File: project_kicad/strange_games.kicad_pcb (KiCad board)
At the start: 2 copper layers, 166 x 166 mm, 210 parts, among them J1 Display, M1 Motor_DC, Q1 Si2302A, Q3 Si2302A, Q4 Q_Photo, SW1 SW_Push, SW10 SW_Push, SW11 SW_Push, SW2 SW_Push, SW3 SW_Push, SW4 SW_Push, SW5 SW_Push, SW6 SW_Push, SW7 SW_Push, SW8 SW_Push, SW9 SW_Push, U1 charge controller, U2 boost converter, U3 LDL1117S33R, U4 ESP32-DEVKIT-V1, U5 TMP112xxDRL, U6 vibrating_sensor, U7 LSM6DS3, U8 MQ-135 gas sensor

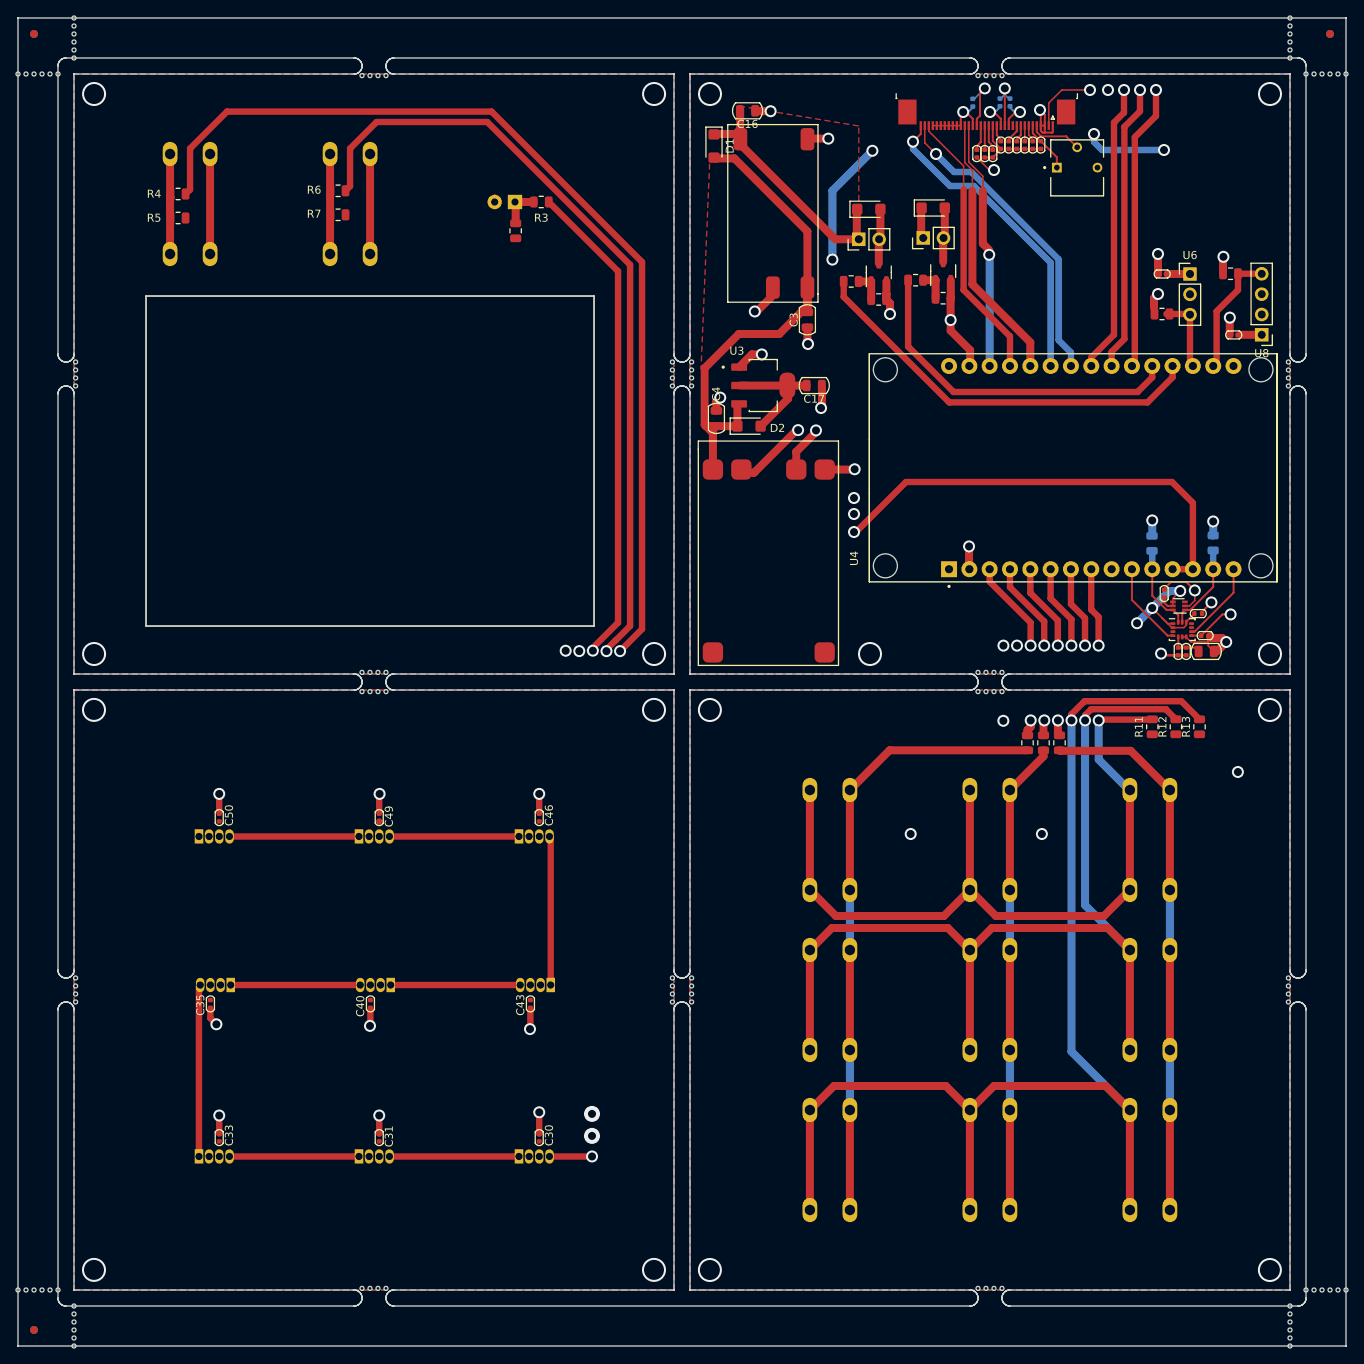
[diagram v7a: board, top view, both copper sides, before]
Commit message: bugfix
In the last version we lost netlist - it was improved
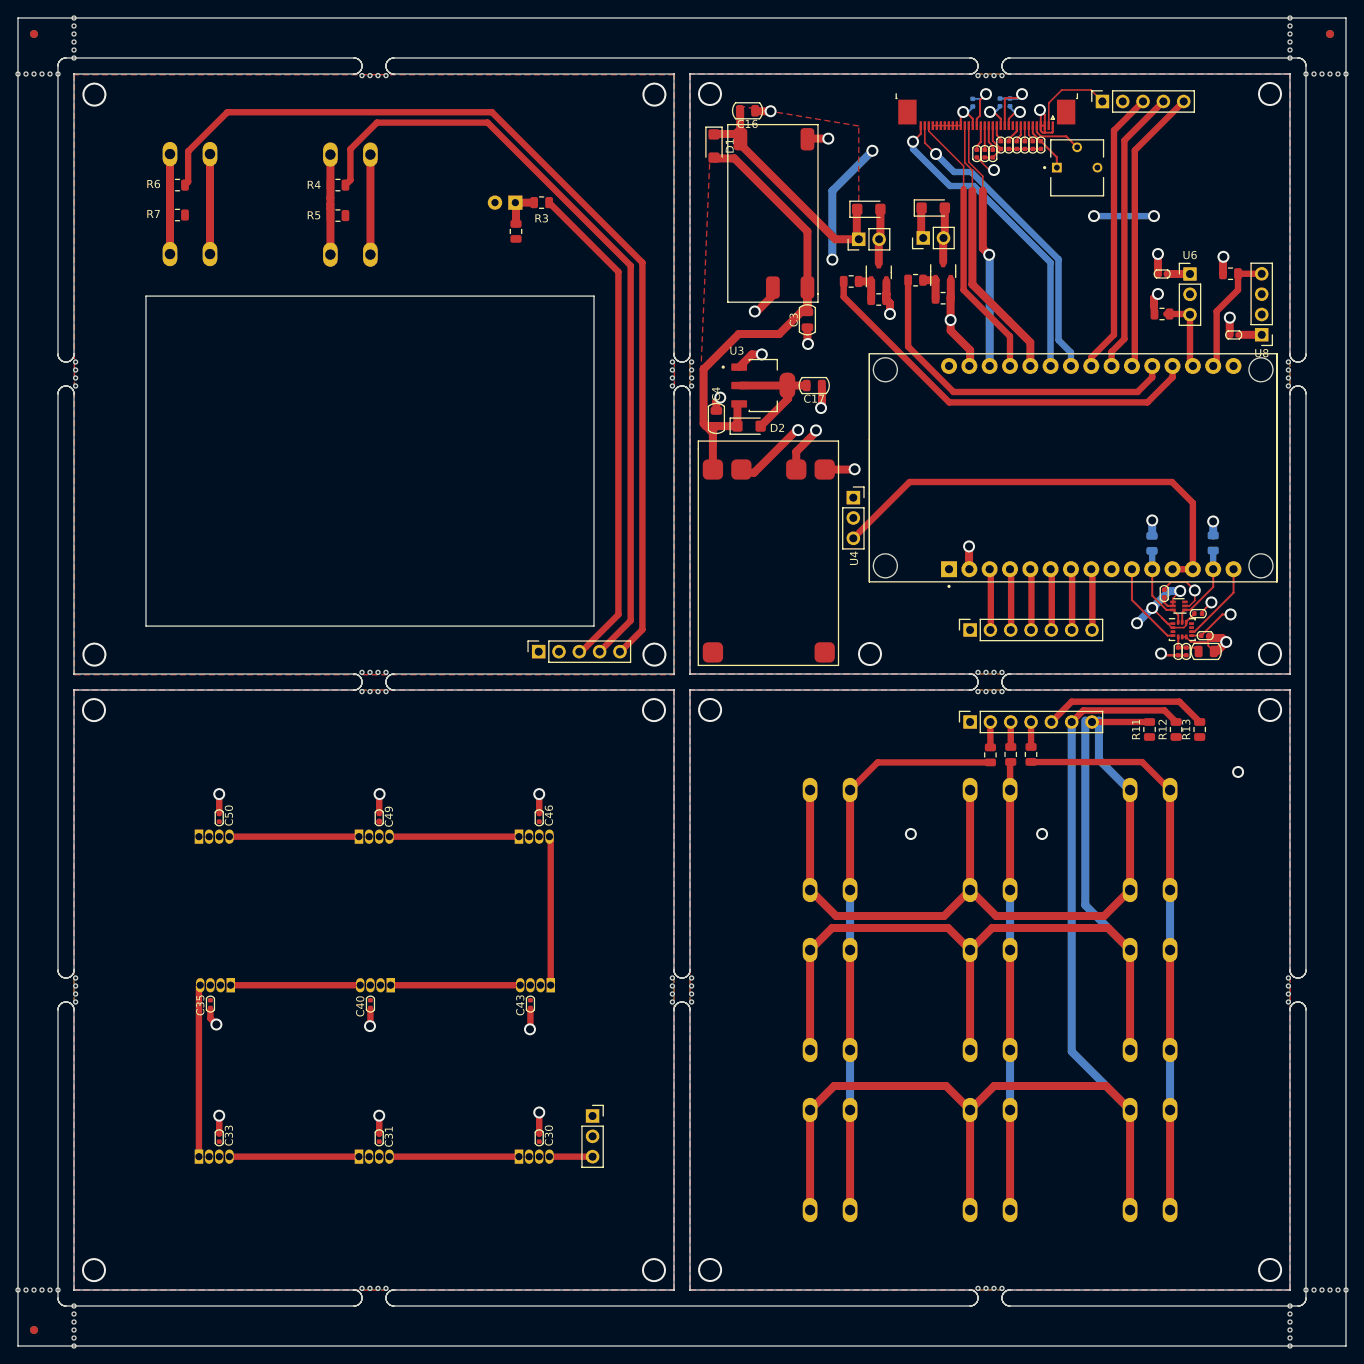
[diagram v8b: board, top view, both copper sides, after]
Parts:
- added REF**: PinSocket_1x07_P2.54mm_Vertical, Connector_PinSocket_2.54mm:PinSocket_1x07_P2.54mm_Vertical, F.Cu at (163.0, 96.5)
- added REF**: PinSocket_1x07_P2.54mm_Vertical, Connector_PinSocket_2.54mm:PinSocket_1x07_P2.54mm_Vertical, F.Cu at (163.0, 108.0)
- added REF**: PinSocket_1x05_P2.54mm_Vertical, Connector_PinSocket_2.54mm:PinSocket_1x05_P2.54mm_Vertical, F.Cu at (109.1, 99.2)
- added REF**: PinSocket_1x03_P2.54mm_Vertical, Connector_PinSocket_2.54mm:PinSocket_1x03_P2.54mm_Vertical, F.Cu at (148.4, 80.0)
- added REF**: PinSocket_1x03_P2.54mm_Vertical, Connector_PinSocket_2.54mm:PinSocket_1x03_P2.54mm_Vertical, F.Cu at (115.8, 157.3)
- added REF**: PinSocket_1x05_P2.54mm_Vertical, Connector_PinSocket_2.54mm:PinSocket_1x05_P2.54mm_Vertical, F.Cu at (179.6, 30.4)
- moved R6 20.1 mm to (63.9, 40.9)
- moved R7 20.1 mm to (63.9, 44.6)
- moved SW1 20.0 mm to (83.1, 37.1)
- moved R4 20.0 mm to (84.0, 40.9)
- moved SW2 20.0 mm to (63.0, 37.0)
- moved R5 20.0 mm to (84.0, 44.7)
- moved R8 4.88 mm to (165.6, 112.1)
- moved R9 4.35 mm to (168.1, 112.1)
- moved R10 3.84 mm to (170.6, 112.1)
- moved R11 0.48 mm to (185.4, 108.9)
- moved R13 0.34 mm to (191.7, 108.9)
- moved R12 0.34 mm to (188.8, 108.9)
- moved R20 0.09 mm to (106.3, 46.7)
- moved R3 0.09 mm to (109.5, 43.1)
- moved Q4 0.09 mm to (106.2, 43.1)
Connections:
- C30 pad 1: (no net) -> GND
- C30 pad 2: (no net) -> +3V3
- C31 pad 1: (no net) -> +3V3
- C31 pad 2: (no net) -> GND
- C33 pad 1: (no net) -> GND
- C33 pad 2: (no net) -> +3V3
- C35 pad 1: (no net) -> +3V3
- C35 pad 2: (no net) -> GND
- C40 pad 1: (no net) -> GND
- C40 pad 2: (no net) -> +3V3
- C43 pad 1: (no net) -> +3V3
- C43 pad 2: (no net) -> GND
- C46 pad 1: (no net) -> GND
- C46 pad 2: (no net) -> +3V3
- C49 pad 1: (no net) -> +3V3
- C49 pad 2: (no net) -> GND
- C50 pad 1: (no net) -> GND
- C50 pad 2: (no net) -> +3V3
- D10 pad 1: (no net) -> Net-(D10-DO)
- D10 pad 2: (no net) -> GND
- D10 pad 3: (no net) -> +3V3
- D10 pad 4: (no net) -> Net-(D10-DI)
- D11 pad 1: (no net) -> Net-(D11-DO)
- D11 pad 2: (no net) -> GND
- D11 pad 3: (no net) -> +3V3
- D11 pad 4: (no net) -> Net-(D10-DO)
- D12 pad 1: (no net) -> Net-(D12-DO)
- D12 pad 2: (no net) -> GND
- D12 pad 3: (no net) -> +3V3
- D12 pad 4: (no net) -> Net-(D11-DO)
- D13 pad 1: (no net) -> unconnected-(D13-DO-Pad1)
- D13 pad 2: (no net) -> GND
- D13 pad 3: (no net) -> +3V3
- D13 pad 4: (no net) -> Net-(D12-DO)
- D5 pad 1: (no net) -> Net-(D5-DO)
- D5 pad 2: (no net) -> GND
- D5 pad 3: (no net) -> +3V3
- D5 pad 4: (no net) -> Luminodiodes
- D6 pad 1: (no net) -> Net-(D6-DO)
- D6 pad 2: (no net) -> GND
- D6 pad 3: (no net) -> +3V3
- D6 pad 4: (no net) -> Net-(D5-DO)
- D7 pad 1: (no net) -> Net-(D7-DO)
- D7 pad 2: (no net) -> GND
- D7 pad 3: (no net) -> +3V3
- D7 pad 4: (no net) -> Net-(D6-DO)
- D8 pad 1: (no net) -> Net-(D8-DO)
- D8 pad 2: (no net) -> GND
- D8 pad 3: (no net) -> +3V3
- D8 pad 4: (no net) -> Net-(D7-DO)
- D9 pad 1: (no net) -> Net-(D10-DI)
- D9 pad 2: (no net) -> GND
- D9 pad 3: (no net) -> +3V3
- D9 pad 4: (no net) -> Net-(D8-DO)
- Q4 pad 1: (no net) -> Net-(Q4-C)
- Q4 pad 2: (no net) -> GND
- R10 pad 1: (no net) -> Net-(R10-Pad1)
- R10 pad 2: (no net) -> BOut3
- R11 pad 1: (no net) -> GND
- R11 pad 2: (no net) -> Bin1
- R12 pad 1: (no net) -> GND
- R12 pad 2: (no net) -> Bin2
- R13 pad 1: (no net) -> GND
- R13 pad 2: (no net) -> Bin3
- R20 pad 1: (no net) -> Net-(Q4-C)
- R20 pad 2: (no net) -> +3V3
- R3 pad 1: (no net) -> Net-(Q4-C)
- R3 pad 2: (no net) -> PhotoSensor
- R4 pad 1: (no net) -> Net-(R4-Pad1)
- R4 pad 2: (no net) -> B1
- R5 pad 1: (no net) -> Net-(R4-Pad1)
- R5 pad 2: (no net) -> +3V3
- R6 pad 1: (no net) -> Net-(R6-Pad1)
- R6 pad 2: (no net) -> B2
- R7 pad 1: (no net) -> Net-(R6-Pad1)
- R7 pad 2: (no net) -> +3V3
- R8 pad 1: (no net) -> Net-(R8-Pad1)
- R8 pad 2: (no net) -> BOut1
- R9 pad 1: (no net) -> Net-(R9-Pad1)
- R9 pad 2: (no net) -> BOut2
- SW1 pad 1: (no net) -> Net-(R4-Pad1)
- SW1 pad 2: (no net) -> GND
- SW10 pad 1: (no net) -> Bin3
- SW10 pad 2: (no net) -> Net-(R9-Pad1)
- SW11 pad 1: (no net) -> Bin3
- SW11 pad 2: (no net) -> Net-(R10-Pad1)
- SW2 pad 1: (no net) -> Net-(R6-Pad1)
- SW2 pad 2: (no net) -> GND
- SW3 pad 1: (no net) -> Bin1
- SW3 pad 2: (no net) -> Net-(R8-Pad1)
- SW4 pad 1: (no net) -> Bin1
- SW4 pad 2: (no net) -> Net-(R9-Pad1)
- SW5 pad 1: (no net) -> Bin1
- SW5 pad 2: (no net) -> Net-(R10-Pad1)
- SW6 pad 1: (no net) -> Bin2
- SW6 pad 2: (no net) -> Net-(R8-Pad1)
- SW7 pad 1: (no net) -> Bin2
- SW7 pad 2: (no net) -> Net-(R9-Pad1)
- SW8 pad 1: (no net) -> Bin2
- SW8 pad 2: (no net) -> Net-(R10-Pad1)
- SW9 pad 1: (no net) -> Bin3
- SW9 pad 2: (no net) -> Net-(R8-Pad1)
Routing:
- net (no net): track 1094.6 -> 0.00 mm, vias 43 -> 16
- net Bin3: track 0.00 -> 154.8 mm
- net Bin2: track 0.00 -> 127.3 mm
- net B2: track 0.00 -> 121.1 mm
- net Bin1: track 0.00 -> 100.4 mm
- net B1: track 0.00 -> 98.4 mm
- net Net-(R8-Pad1): track 0.00 -> 71.5 mm
- net Net-(R10-Pad1): track 0.00 -> 71.3 mm
- net PhotoSensor: track 0.00 -> 61.9 mm
- net Net-(R9-Pad1): track 0.00 -> 56.0 mm
- net GND: track 0.00 -> 45.8 mm, vias 0 -> 12
- net Net-(D7-DO): track 0.00 -> 21.7 mm
- net Net-(D10-DO): track 0.00 -> 18.9 mm
- net Net-(D8-DO): track 0.00 -> 16.2 mm
- net Net-(D6-DO): track 0.00 -> 16.2 mm
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- added copper zone on F.Cu, net +3V3
- added copper zone on B.Cu, net GND
- added copper zone on F.Cu, net GND
- removed copper zone on B.Cu, net (none)
- removed copper zone on F.Cu, net (none)
